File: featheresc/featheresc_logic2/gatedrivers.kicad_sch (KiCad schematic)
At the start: 8 parts, among them U4 NCP81155MN, U5 NCP81155MN

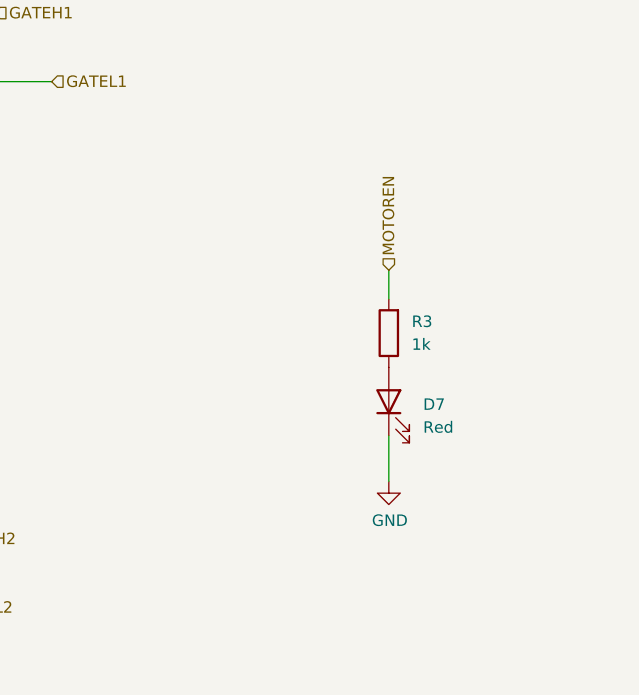
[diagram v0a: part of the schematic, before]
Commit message: Update layout to be more compact, swap a few parts
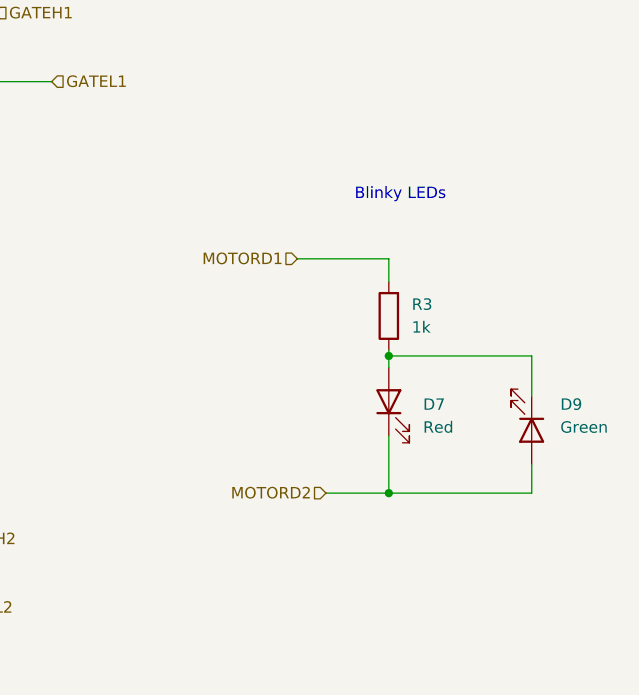
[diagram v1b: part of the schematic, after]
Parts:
- added D9: Green, LED_SMD:LED_0805_2012Metric_Pad1.15x1.40mm_HandSolder, symbol Device:LED
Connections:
- net GND: no longer D7.1 (K)
- net MOTORD1: now also R3.2
- net MOTORD2: now also D7.1 (K), D9.2 (A)
- net MOTOREN: no longer R3.2
- net at D7.2 (A), R3.1: now also D9.1 (K)
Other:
- note added: "Blinky LEDs"
- moved on the sheet: R3
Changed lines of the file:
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@@
   (junction (at 68.58 53.34) (diameter 0.9144) (color 0 0 0 0)
   )
+  (junction (at 161.29 123.19) (diameter 0) (color 0 0 0 0)
+  )
+  (junction (at 161.29 107.95) (diameter 0) (color 0 0 0 0)
+  )
   (junction (at 68.58 146.685) (diameter 0.9144) (color 0 0 0 0)
   )
@@
   (junction (at 68.58 86.995) (diameter 0.9144) (color 0 0 0 0)
   )
+  (wire (pts (xy 161.29 107.95) (xy 161.29 109.22))
+    (stroke (width 0) (type default) (color 0 0 0 0))
+  )
+  (wire (pts (xy 161.29 116.84) (xy 161.29 123.19))
+    (stroke (width 0) (type default) (color 0 0 0 0))
+  )
   (wire (pts (xy 68.58 142.24) (xy 68.58 146.685))
     (stroke (width 0) (type solid) (color 0 0 0 0))
   )
+  (wire (pts (xy 161.29 107.315) (xy 161.29 107.95))
+    (stroke (width 0) (type default) (color 0 0 0 0))
+  )
   (wire (pts (xy 65.405 86.995) (xy 68.58 86.995))
     (stroke (width 0) (type solid) (color 0 0 0 0))
@@
     (stroke (width 0) (type solid) (color 0 0 0 0))
   )
+  (wire (pts (xy 177.165 107.95) (xy 177.165 112.395))
+    (stroke (width 0) (type default) (color 0 0 0 0))
+  )
   (wire (pts (xy 68.58 113.03) (xy 68.58 118.11))
     (stroke (width 0) (type solid) (color 0 0 0 0))
@@
     (stroke (width 0) (type solid) (color 0 0 0 0))
   )
-  (wire (pts (xy 161.29 116.84) (xy 161.29 121.92))
-    (stroke (width 0) (type default) (color 0 0 0 0))
-  )
   (wire (pts (xy 89.535 132.08) (xy 89.535 123.19))
     (stroke (width 0) (type solid) (color 0 0 0 0))
   )
+  (wire (pts (xy 161.29 107.95) (xy 177.165 107.95))
+    (stroke (width 0) (type default) (color 0 0 0 0))
+  )
   (wire (pts (xy 78.105 128.27) (xy 111.125 128.27))
     (stroke (width 0) (type solid) (color 0 0 0 0))
@@
     (stroke (width 0) (type solid) (color 0 0 0 0))
   )
+  (wire (pts (xy 151.13 97.155) (xy 161.29 97.155))
+    (stroke (width 0) (type default) (color 0 0 0 0))
+  )
+  (wire (pts (xy 161.29 123.19) (xy 154.305 123.19))
+    (stroke (width 0) (type default) (color 0 0 0 0))
+  )
   (wire (pts (xy 68.58 109.22) (xy 68.58 113.03))
     (stroke (width 0) (type solid) (color 0 0 0 0))
@@
     (stroke (width 0) (type solid) (color 0 0 0 0))
   )
-  (wire (pts (xy 161.29 98.425) (xy 161.29 101.6))
+  (wire (pts (xy 161.29 97.155) (xy 161.29 99.695))
     (stroke (width 0) (type default) (color 0 0 0 0))
   )
@@
     (stroke (width 0) (type solid) (color 0 0 0 0))
   )
+  (wire (pts (xy 177.165 123.19) (xy 161.29 123.19))
+    (stroke (width 0) (type default) (color 0 0 0 0))
+  )
   (wire (pts (xy 78.105 64.77) (xy 83.82 64.77))
     (stroke (width 0) (type solid) (color 0 0 0 0))
@@
     (stroke (width 0) (type solid) (color 0 0 0 0))
   )
+  (wire (pts (xy 177.165 120.015) (xy 177.165 123.19))
+    (stroke (width 0) (type default) (color 0 0 0 0))
+  )
   (wire (pts (xy 68.58 88.9) (xy 68.58 86.995))
     (stroke (width 0) (type solid) (color 0 0 0 0))
@@
   (wire (pts (xy 65.405 146.685) (xy 68.58 146.685))
     (stroke (width 0) (type solid) (color 0 0 0 0))
+  )
+  (text "Blinky LEDs" (at 157.48 90.805 0)
+    (effects (font (size 1.27 1.27)) (justify left bottom))
   )
   (label "BOOST1" (at 89.535 53.34 180)
@@
     (effects (font (size 1.27 1.27)) (justify left))
   )
+  (hierarchical_label "MOTORD1" (shape input) (at 151.13 97.155 180)
+    (effects (font (size 1.27 1.27)) (justify right))
+  )
   (hierarchical_label "MOTORD1" (shape input) (at 59.69 67.31 180)
     (effects (font (size 1.27 1.27)) (justify right))
@@
     (effects (font (size 1.27 1.27)) (justify right))
   )
-  (hierarchical_label "MOTOREN" (shape input) (at 161.29 98.425 90)
-    (effects (font (size 1.27 1.27)) (justify left))
-  )
   (hierarchical_label "PHASE2" (shape input) (at 89.535 132.08 0)
     (effects (font (size 1.27 1.27)) (justify left))
@@
     (effects (font (size 1.27 1.27)) (justify left))
   )
-  (symbol (lib_id "Device:R") (at 161.29 105.41 180)
+  (hierarchical_label "MOTORD2" (shape input) (at 154.305 123.19 180)
+    (effects (font (size 1.27 1.27)) (justify right))
+  )
+  (symbol (lib_id "Device:LED") (at 177.165 116.205 270)
     (in_bom yes) (on_board yes) (fields_autoplaced)
-    (property "Reference" "R3" (id 0) (at 163.83 104.1399 0)
+    (property "Reference" "D9" (id 0) (at 180.34 113.3474 90)
+      (effects (font (size 1.27 1.27)) (justify left))
+    )
+    (property "Value" "Green" (id 1) (at 180.34 115.8874 90)
+      (effects (font (size 1.27 1.27)) (justify left))
+    )
+    (property "Footprint" "LED_SMD:LED_0805_2012Metric_Pad1.15x1.40mm_HandSolder" (id 2) (at 177.165 116.205 0)
+      (effects (font (size 1.27 1.27)) hide)
+    )
+    (property "Datasheet" "~" (id 3) (at 177.165 116.205 0)
+      (effects (font (size 1.27 1.27)) hide)
+    )
+    (pin "1")
+    (pin "2")
+  )
+  (symbol (lib_id "Device:R") (at 161.29 103.505 180)
+    (in_bom yes) (on_board yes) (fields_autoplaced)
+    (property "Reference" "R3" (id 0) (at 163.83 102.2349 0)
       (effects (font (size 1.27 1.27)) (justify right))
     )
-    (property "Value" "1k" (id 1) (at 163.83 106.6799 0)
+    (property "Value" "1k" (id 1) (at 163.83 104.7749 0)
       (effects (font (size 1.27 1.27)) (justify right))
     )
-    (property "Footprint" "Resistor_SMD:R_0603_1608Metric_Pad0.98x0.95mm_HandSolder" (id 2) (at 163.068 105.41 90)
-      (effects (font (size 1.27 1.27)) hide)
-    )
-    (property "Datasheet" "~" (id 3) (at 161.29 105.41 0)
+    (property "Footprint" "Resistor_SMD:R_0603_1608Metric_Pad0.98x0.95mm_HandSolder" (id 2) (at 163.068 103.505 90)
+      (effects (font (size 1.27 1.27)) hide)
+    )
+    (property "Datasheet" "~" (id 3) (at 161.29 103.505 0)
       (effects (font (size 1.27 1.27)) hide)
     )
@@
     (pin "9")
   )
-  (symbol (lib_id "power:GND") (at 161.29 121.92 0)
-    (in_bom yes) (on_board yes)
-    (property "Reference" "#PWR05" (id 0) (at 161.29 128.27 0)
-      (effects (font (size 1.27 1.27)) hide)
-    )
-    (property "Value" "GND" (id 1) (at 161.4043 126.2444 0))
-    (property "Footprint" "" (id 2) (at 161.29 121.92 0)
-      (effects (font (size 1.27 1.27)) hide)
-    )
-    (property "Datasheet" "" (id 3) (at 161.29 121.92 0)
-      (effects (font (size 1.27 1.27)) hide)
-    )
-    (pin "1")
-  )
   (symbol (lib_id "Device:LED") (at 161.29 113.03 90)

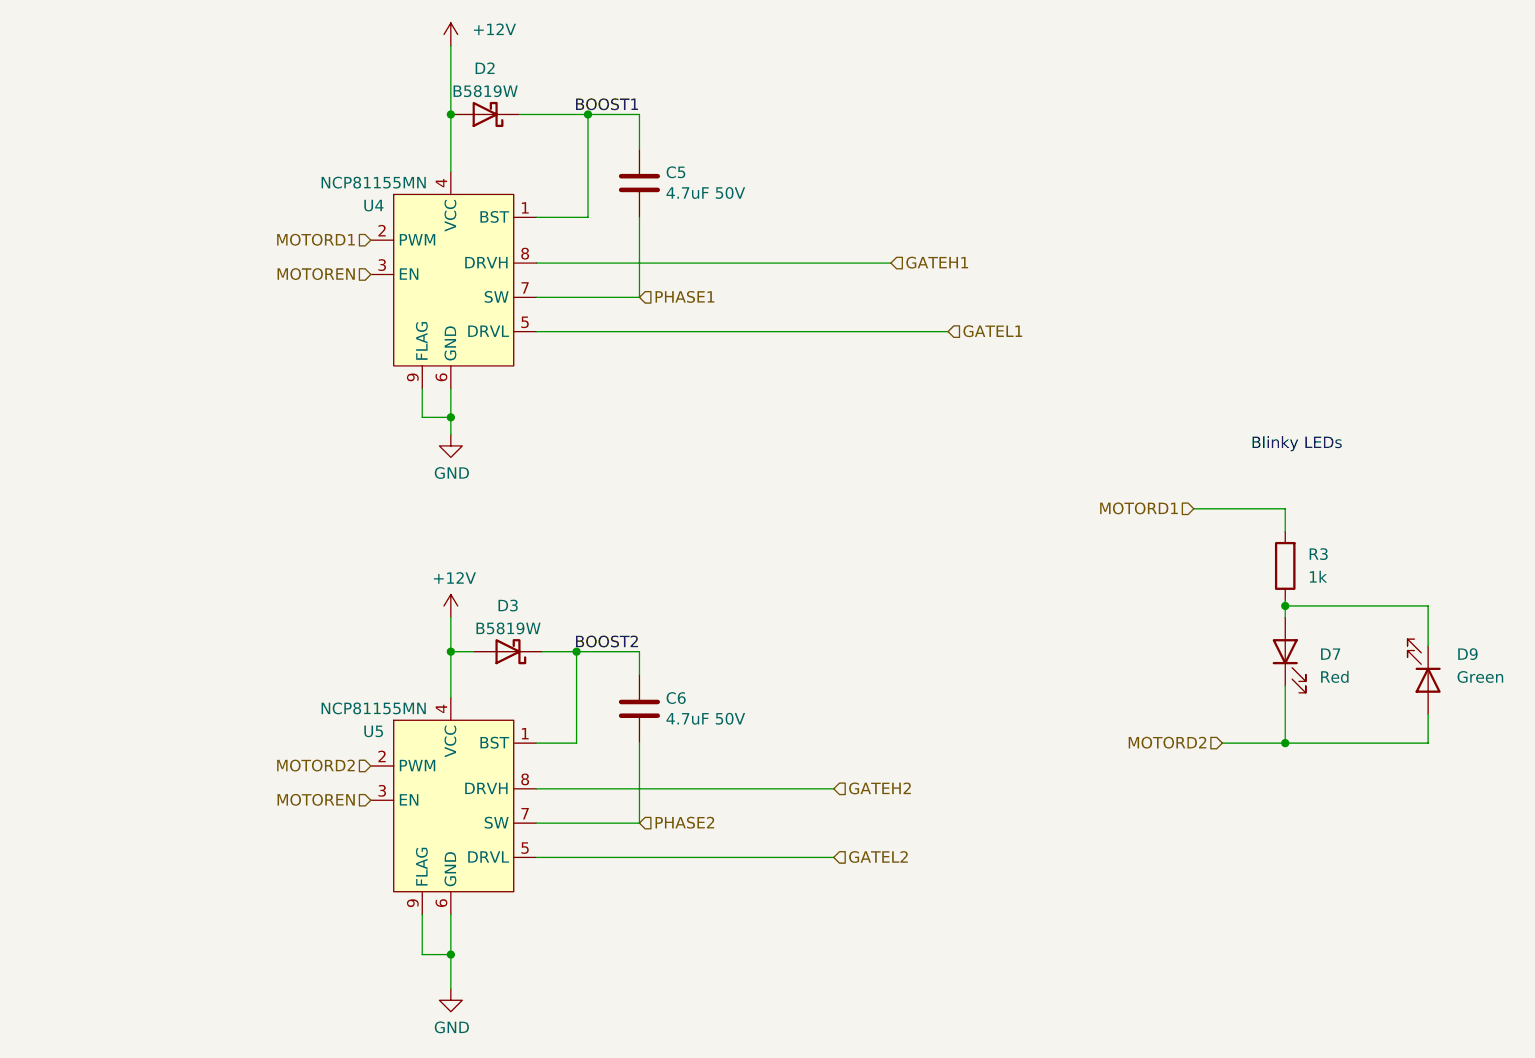
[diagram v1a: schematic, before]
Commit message: improve interconnect pinouts
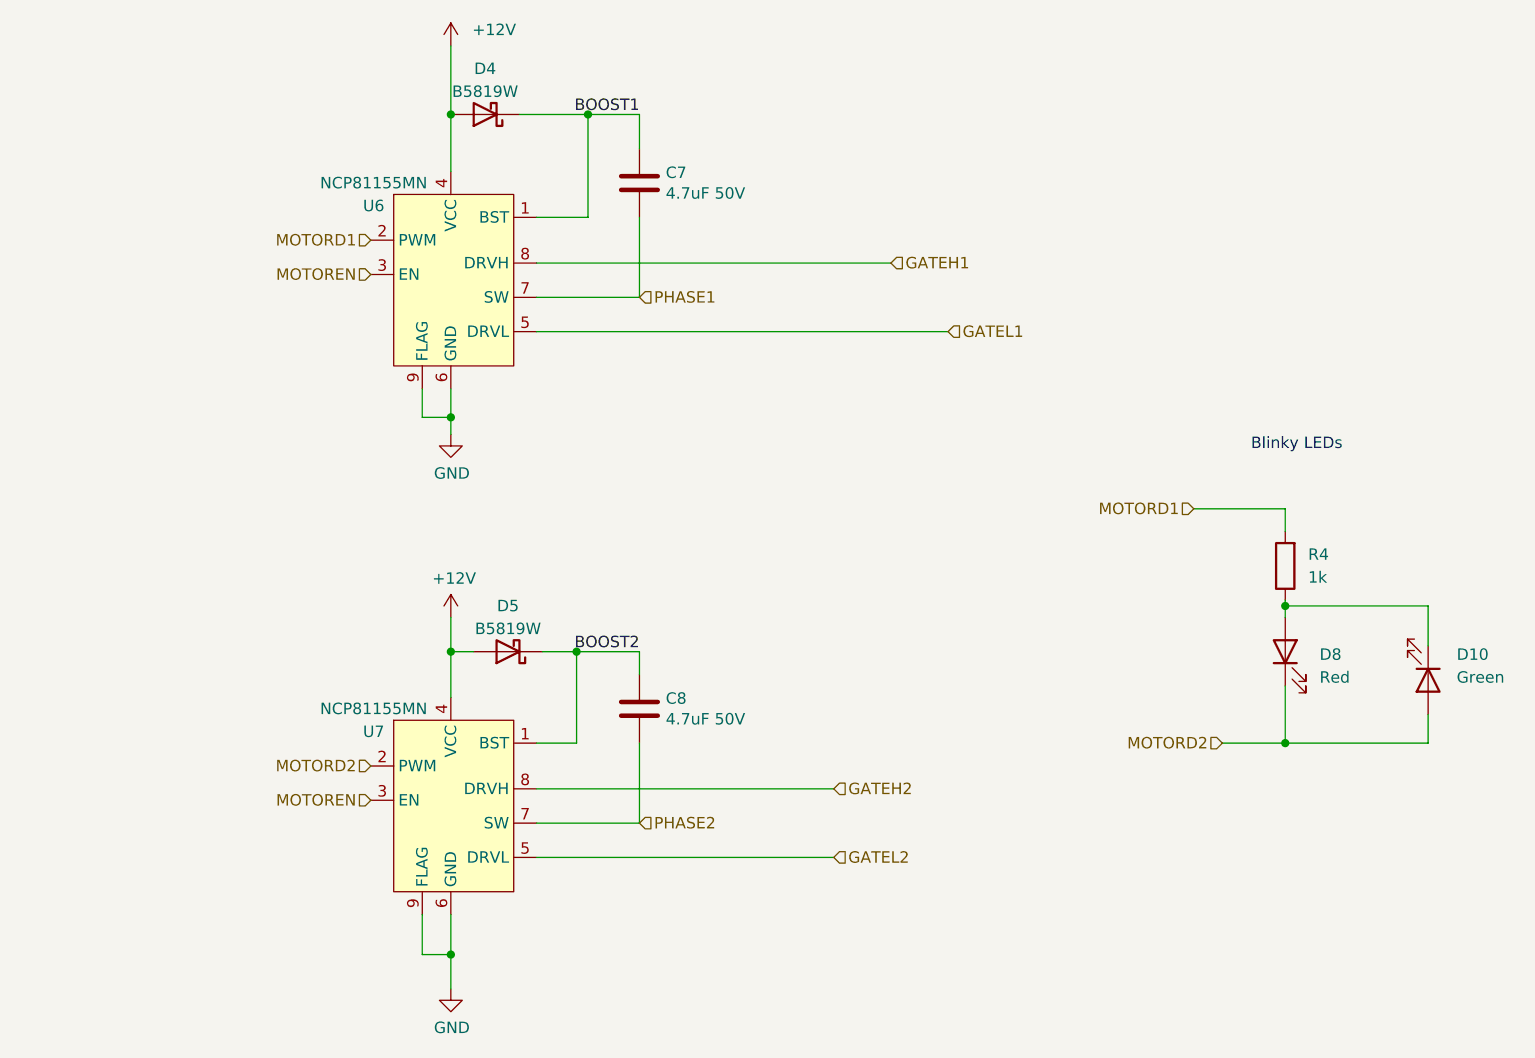
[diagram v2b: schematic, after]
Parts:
- renumbered C5 to C7, C6 to C8, D9 to D10, D2 to D4, D3 to D5, D7 to D8, R3 to R4, U4 to U6, U5 to U7
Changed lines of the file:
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@@
   (symbol (lib_id "Device:LED") (at 177.165 116.205 270)
     (in_bom yes) (on_board yes) (fields_autoplaced)
-    (property "Reference" "D9" (id 0) (at 180.34 113.3474 90)
+    (property "Reference" "D10" (id 0) (at 180.34 113.3474 90)
       (effects (font (size 1.27 1.27)) (justify left))
     )
@@
   (symbol (lib_id "Device:R") (at 161.29 103.505 180)
     (in_bom yes) (on_board yes) (fields_autoplaced)
-    (property "Reference" "R3" (id 0) (at 163.83 102.2349 0)
+    (property "Reference" "R4" (id 0) (at 163.83 102.2349 0)
       (effects (font (size 1.27 1.27)) (justify right))
     )
@@
   (symbol (lib_id "Device:C") (at 89.535 119.38 0)
     (in_bom yes) (on_board yes)
-    (property "Reference" "C6" (id 0) (at 92.456 118.231 0)
+    (property "Reference" "C8" (id 0) (at 92.456 118.231 0)
       (effects (font (size 1.27 1.27)) (justify left))
     )
@@
   (symbol (lib_id "featheresc_logic:NCP81155MN") (at 68.58 132.08 0)
     (in_bom yes) (on_board yes)
-    (property "Reference" "U5" (id 0) (at 60.0075 121.92 0))
+    (property "Reference" "U7" (id 0) (at 60.0075 121.92 0))
     (property "Value" "NCP81155MN" (id 1) (at 60.0075 119.38 0))
     (property "Footprint" "Package_DFN_QFN:DFN-8-1EP_3x3mm_P0.5mm_EP1.66x2.38mm" (id 2) (at 68.58 132.08 0)
@@
   (symbol (lib_id "Device:LED") (at 161.29 113.03 90)
     (in_bom yes) (on_board yes) (fields_autoplaced)
-    (property "Reference" "D7" (id 0) (at 165.1 113.3474 90)
+    (property "Reference" "D8" (id 0) (at 165.1 113.3474 90)
       (effects (font (size 1.27 1.27)) (justify right))
     )
@@
   (symbol (lib_id "power:GND") (at 68.58 88.9 0)
     (in_bom yes) (on_board yes)
-    (property "Reference" "#PWR09" (id 0) (at 68.58 95.25 0)
+    (property "Reference" "#PWR013" (id 0) (at 68.58 95.25 0)
       (effects (font (size 1.27 1.27)) hide)
     )
@@
   (symbol (lib_id "Device:C") (at 89.535 60.96 0)
     (in_bom yes) (on_board yes)
-    (property "Reference" "C5" (id 0) (at 92.4561 59.8106 0)
+    (property "Reference" "C7" (id 0) (at 92.4561 59.8106 0)
       (effects (font (size 1.27 1.27)) (justify left))
     )
@@
   (symbol (lib_id "power:GND") (at 68.58 150.495 0)
     (in_bom yes) (on_board yes)
-    (property "Reference" "#PWR011" (id 0) (at 68.58 156.845 0)
+    (property "Reference" "#PWR015" (id 0) (at 68.58 156.845 0)
       (effects (font (size 1.27 1.27)) hide)
     )
@@
   (symbol (lib_id "power:+12V") (at 68.58 109.22 0)
     (in_bom yes) (on_board yes)
-    (property "Reference" "#PWR010" (id 0) (at 68.58 113.03 0)
+    (property "Reference" "#PWR014" (id 0) (at 68.58 113.03 0)
       (effects (font (size 1.27 1.27)) hide)
     )
@@
   (symbol (lib_id "Device:D_Schottky") (at 72.39 53.34 180)
     (in_bom yes) (on_board yes) (fields_autoplaced)
-    (property "Reference" "D2" (id 0) (at 72.39 48.26 0))
+    (property "Reference" "D4" (id 0) (at 72.39 48.26 0))
     (property "Value" "B5819W" (id 1) (at 72.39 50.8 0))
     (property "Footprint" "Diode_SMD:D_SOD-123" (id 2) (at 72.39 53.34 0)
@@
   (symbol (lib_id "featheresc_logic:NCP81155MN") (at 68.58 73.66 0)
     (in_bom yes) (on_board yes)
-    (property "Reference" "U4" (id 0) (at 60.0075 63.5 0))
+    (property "Reference" "U6" (id 0) (at 60.0075 63.5 0))
     (property "Value" "NCP81155MN" (id 1) (at 60.0075 60.96 0))
     (property "Footprint" "Package_DFN_QFN:DFN-8-1EP_3x3mm_P0.5mm_EP1.66x2.38mm" (id 2) (at 68.58 73.66 0)
@@
   (symbol (lib_id "power:+12V") (at 68.58 45.72 0)
     (in_bom yes) (on_board yes)
-    (property "Reference" "#PWR08" (id 0) (at 68.58 49.53 0)
+    (property "Reference" "#PWR012" (id 0) (at 68.58 49.53 0)
       (effects (font (size 1.27 1.27)) hide)
     )
@@
   (symbol (lib_id "Device:D_Schottky") (at 74.93 113.03 180)
     (in_bom yes) (on_board yes) (fields_autoplaced)
-    (property "Reference" "D3" (id 0) (at 74.93 107.95 0))
+    (property "Reference" "D5" (id 0) (at 74.93 107.95 0))
     (property "Value" "B5819W" (id 1) (at 74.93 110.49 0))
     (property "Footprint" "Diode_SMD:D_SOD-123" (id 2) (at 74.93 113.03 0)
